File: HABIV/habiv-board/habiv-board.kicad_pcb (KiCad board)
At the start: 4 copper layers, 102 parts, among them IC1 RTC_PCF8523T, J1 Micro_SD_Card_Det, J2 Conn_ARM_JTAG_SWD_20, J3 Conn_01x02_Male, J4 Conn_01x16_Male, J5 Conn_01x02_Male, J6 Conn_01x16_Male, J7 Conn_01x16_Male, J9 Conn_01x02_Male, Q1 32.768KHz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

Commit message: finish submodules and combine
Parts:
- removed B1: CR1220, Adafruit Ultimate GPS:CR1220
- added C11: 100n, Capacitor_SMD:C_0805_2012Metric, F.Cu at (214.6, 105.4)
- added C12: 100n, Capacitor_SMD:C_0805_2012Metric, F.Cu at (218.7, 101.9)
- added C15: 10u, Capacitor_SMD:C_0805_2012Metric, F.Cu at (214.6, 107.4)
- added C18: 10n, Capacitor_SMD:C_0805_2012Metric, F.Cu at (218.0, 105.4)
- added C19: 100n, Capacitor_SMD:C_0805_2012Metric, F.Cu at (222.1, 101.9)
- added R29: 1K, Resistor_SMD:R_0805_2012Metric, F.Cu at (218.0, 107.4)
- added R30: 1K, Resistor_SMD:R_0805_2012Metric, F.Cu at (221.4, 103.8)
- added R32: 0, Resistor_SMD:R_0805_2012Metric, F.Cu at (225.5, 101.9)
- added R33: 0, Resistor_SMD:R_0805_2012Metric, F.Cu at (221.4, 105.8)
- added R37: 0, Resistor_SMD:R_0805_2012Metric, F.Cu at (224.8, 103.8)
- added U6: LSM9DS1TR, digikey-footprints:LGA-24_3x3.5mm_LSM9DS1, F.Cu at (209.9, 100.2)
- 10k4: value R5 -> R8; footprint Resistors_SMD:R_0603_HandSoldering -> Resistor_SMD:R_0805_2012Metric
- B2: footprint Battery:S8411-45R -> S8411-45R:S8411-45R
- D2: value CUS520 -> LED; footprint Adafruit Ultimate GPS:SOD-323 -> LED_SMD:LED_0805_2012Metric
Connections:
- 10k4 pad 1: (no net) -> GND
- 10k4 pad 2: GND -> Net-(10k4-Pad2)
- D1 pad C: (no net) -> PB6
- IC1 pad 7: (no net) -> Net-(IC1-Pad7)
- J1 pad 10: (no net) -> Net-(J1-Pad10)
- J1 pad 9: (no net) -> Net-(J1-Pad9)
- J7 pad 15: (no net) -> Net-(J7-Pad15)
- R20 pad 2: (no net) -> PC7
- R21 pad 2: (no net) -> PA5
- R22 pad 2: (no net) -> PA6
- R26 pad 2: (no net) -> PB15
- R27 pad 2: (no net) -> PA10
- U1 pad 5: (no net) -> Net-(U1-Pad5)
- U1 pad 6: (no net) -> Net-(U1-Pad6)
- U3 pad P$13: (no net) -> /1PPS
- U3 pad P$14: (no net) -> Net-(U3-PadP$14)
- U3 pad P$15: (no net) -> Net-(U3-PadP$15)
- U3 pad P$16: (no net) -> Net-(U3-PadP$16)
- U3 pad P$17: (no net) -> Net-(U3-PadP$17)
- U3 pad P$18: (no net) -> Net-(U3-PadP$18)
- U3 pad P$2: (no net) -> Net-(U3-PadP$2)
- U3 pad P$20: (no net) -> Net-(U3-PadP$20)
- U3 pad P$6: (no net) -> Net-(U3-PadP$6)
- U3 pad P$7: (no net) -> Net-(U3-PadP$7)
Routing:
- net +3V3: track 141.7 -> 183.0 mm, vias 12 -> 13
- net Net-(B1-Pad+$1): track 41.3 -> 0.00 mm, vias 1 -> 0
- net GND: track 414.3 -> 411.7 mm
- net /VBACKUP: track 16.9 -> 15.6 mm

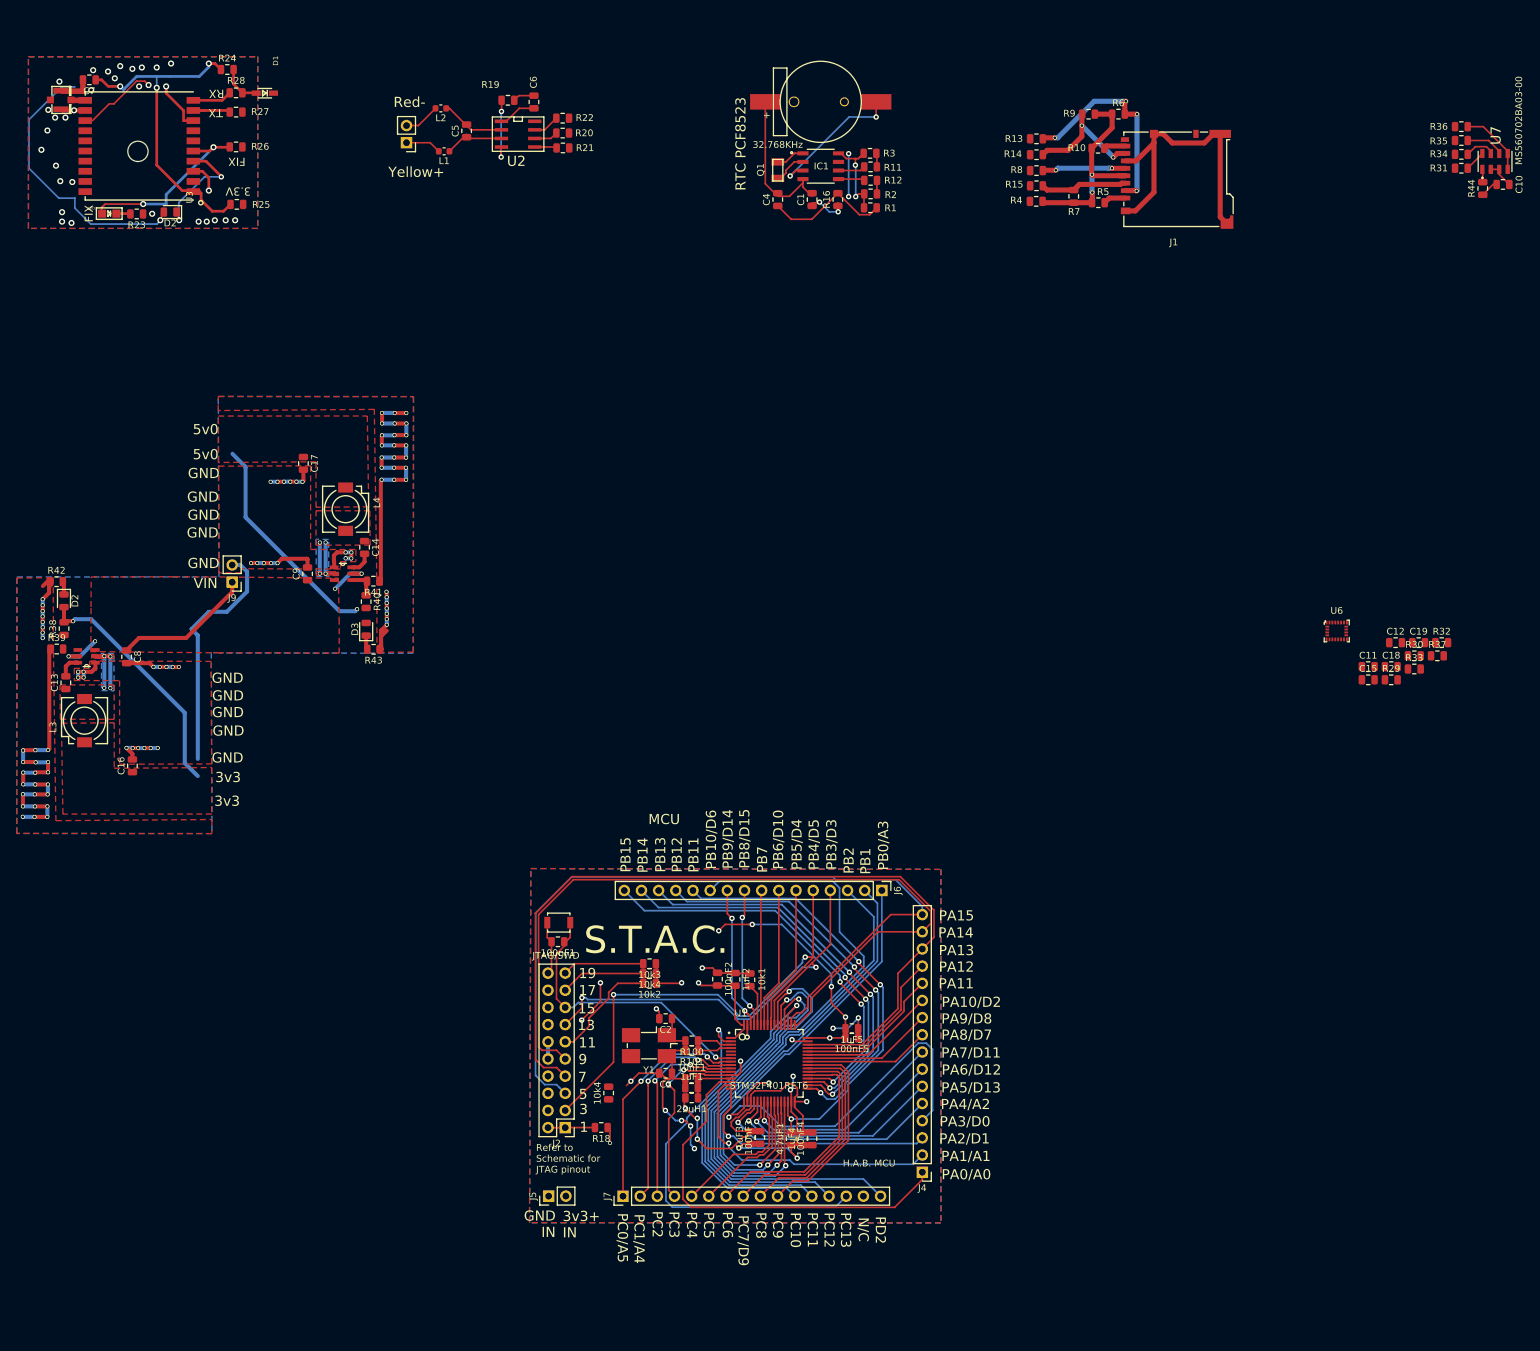
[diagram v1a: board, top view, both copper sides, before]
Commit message: layout for imu
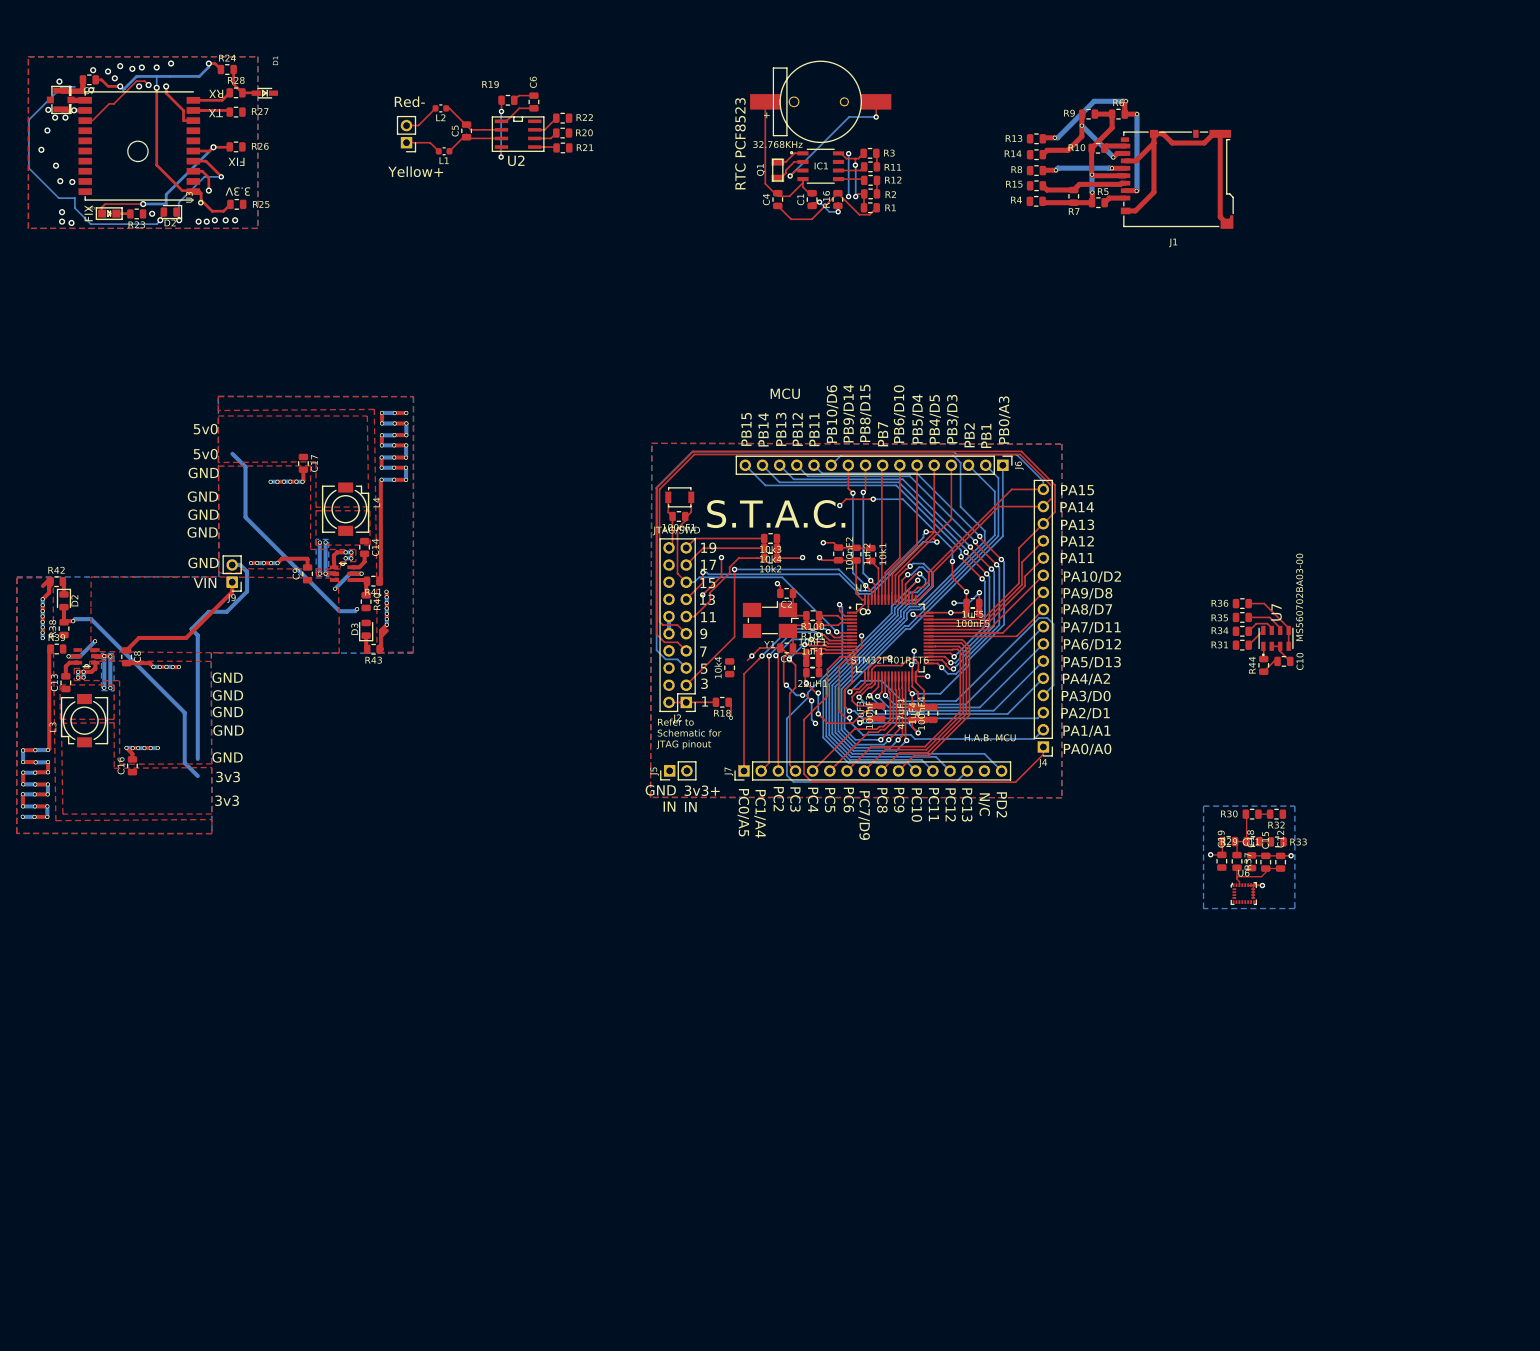
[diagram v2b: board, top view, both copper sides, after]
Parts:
- moved C10 77.6 mm to (202.1, 104.7)
- moved R34 77.6 mm to (196.0, 100.2)
- moved R35 77.6 mm to (196.0, 98.2)
- moved R44 77.6 mm to (199.2, 105.2)
- moved U7 77.6 mm to (201.0, 101.2)
- moved R31 77.6 mm to (196.0, 102.2)
- moved R36 77.6 mm to (196.0, 96.1)
- moved J6 65.4 mm to (160.6, 75.6)
- moved 100nF2 65.4 mm to (136.2, 88.8)
- moved 100nF3 65.4 mm to (142.5, 112.2)
- moved 100nF4 65.4 mm to (150.2, 112.4)
- moved 100nF5 65.4 mm to (156.1, 97.4)
- moved 10k1 65.4 mm to (141.1, 88.8)
- moved 10k4 65.4 mm to (126.2, 87.9)
- moved 10k4 65.4 mm to (120.2, 105.6)
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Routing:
- net GND: track 411.7 -> 427.0 mm, vias 136 -> 139
- net Net-(C12-Pad1): track 0.00 -> 10.0 mm
- net +3V3: track 183.0 -> 191.1 mm
- net PB9: track 23.3 -> 25.1 mm
- net PB8: track 22.8 -> 24.5 mm
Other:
- net class Default: trace_width 0.25 -> 0.2

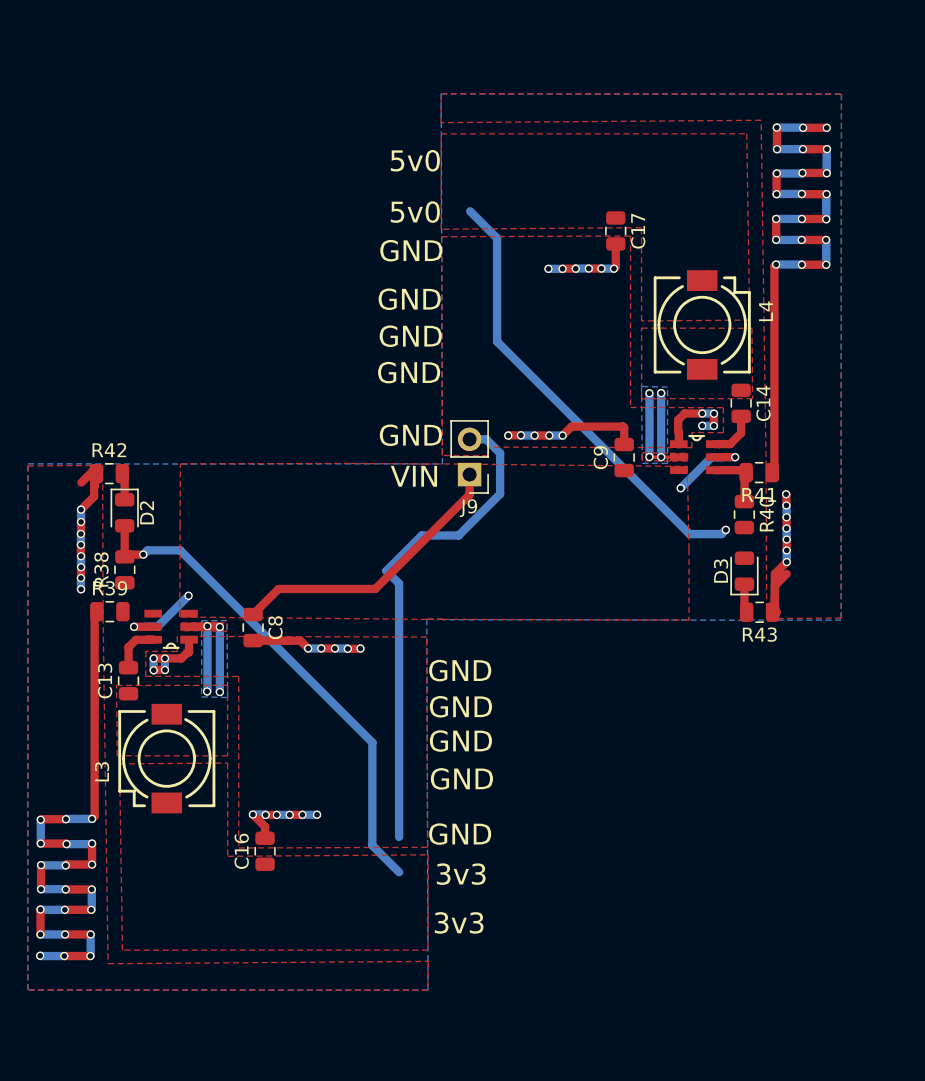
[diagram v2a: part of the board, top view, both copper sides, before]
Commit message: fix power system layout on habiv
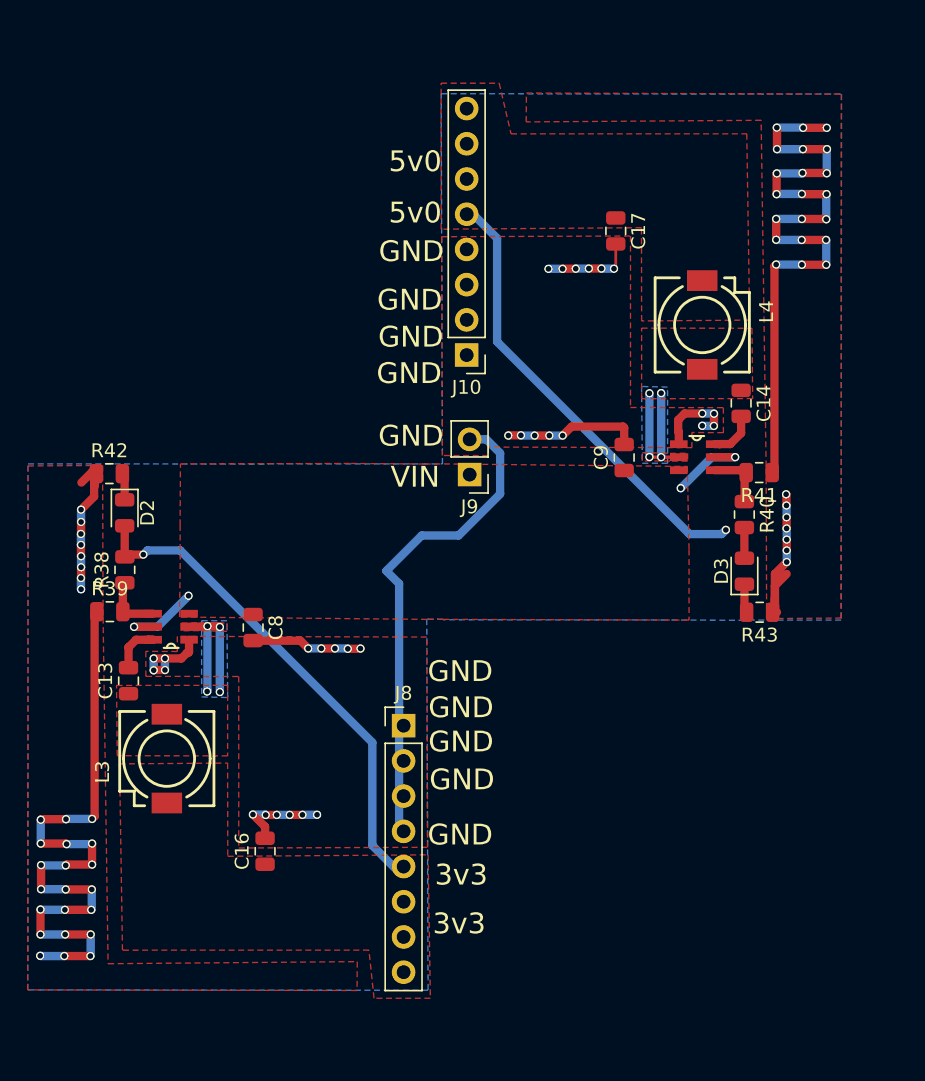
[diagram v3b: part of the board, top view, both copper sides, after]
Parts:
- added J10: Conn_01x08_Male, Connector_PinHeader_2.54mm:PinHeader_1x08_P2.54mm_Vertical, F.Cu at (46.4, 84.3)
- added J8: Conn_01x08_Male, Connector_PinHeader_2.54mm:PinHeader_1x08_P2.54mm_Vertical, F.Cu at (41.8, 111.0)
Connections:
- IC1 pad 7: Net-(IC1-Pad7) -> (no net)
- J1 pad 10: Net-(J1-Pad10) -> (no net)
- J1 pad 9: Net-(J1-Pad9) -> (no net)
- J7 pad 15: Net-(J7-Pad15) -> (no net)
- U1 pad 5: Net-(U1-Pad5) -> (no net)
- U1 pad 6: Net-(U1-Pad6) -> (no net)
- U3 pad P$13: /1PPS -> (no net)
- U3 pad P$14: Net-(U3-PadP$14) -> (no net)
- U3 pad P$15: Net-(U3-PadP$15) -> (no net)
- U3 pad P$16: Net-(U3-PadP$16) -> (no net)
- U3 pad P$17: Net-(U3-PadP$17) -> (no net)
- U3 pad P$18: Net-(U3-PadP$18) -> (no net)
- U3 pad P$2: Net-(U3-PadP$2) -> (no net)
- U3 pad P$20: Net-(U3-PadP$20) -> (no net)
- U3 pad P$4: /VBACKUP -> (no net)
- U3 pad P$6: Net-(U3-PadP$6) -> (no net)
- U3 pad P$7: Net-(U3-PadP$7) -> (no net)
- U6 pad 10: Net-(U6-Pad10) -> (no net)
- U6 pad 11: Net-(U6-Pad11) -> (no net)
- U6 pad 12: Net-(U6-Pad12) -> (no net)
- U6 pad 13: Net-(U6-Pad13) -> (no net)
- U6 pad 5: Net-(U6-Pad5) -> (no net)
- U6 pad 6: Net-(U6-Pad6) -> (no net)
- U6 pad 7: Net-(U6-Pad7) -> (no net)
- U6 pad 8: Net-(U6-Pad8) -> (no net)
- U6 pad 9: Net-(U6-Pad9) -> (no net)
- Y1 pad 2: Net-(Y1-Pad2) -> (no net)
- Y1 pad 3: Net-(Y1-Pad3) -> (no net)
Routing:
- net +5V: track 0.00 -> 34.8 mm, vias 0 -> 1
- net Net-(C21-Pad1): track 32.6 -> 0.00 mm, vias 1 -> 0
- net Net-(C8-Pad1): track 33.3 -> 12.7 mm
- net /VBACKUP: track 15.6 -> 0.00 mm, vias 2 -> 0
- net (no net): track 6.70 -> 22.3 mm, vias 2 -> 4
- net Net-(R38-Pad1): track 0.00 -> 4.39 mm
- added copper zone on F.Cu, net +3V3
- added copper zone on F.Cu, net +5V
- added copper zone on F.Cu, net Net-(C13-Pad1)
- added copper zone on F.Cu, net Net-(C14-Pad1)
- added copper zone on F.Cu, net Net-(C8-Pad1)
- removed copper zone on F.Cu, net Net-(C16-Pad1)
- removed copper zone on B.Cu, net Net-(C16-Pad2)
- removed copper zone on F.Cu, net Net-(C16-Pad2)
- removed copper zone on F.Cu, net Net-(C18-Pad1)
- removed copper zone on F.Cu, net Net-(C21-Pad1)
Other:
- net class Default: trace_width 0.2 -> 0.6
